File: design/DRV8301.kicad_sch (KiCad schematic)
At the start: 40 parts, among them U2 LM3671, U3 DRV8301

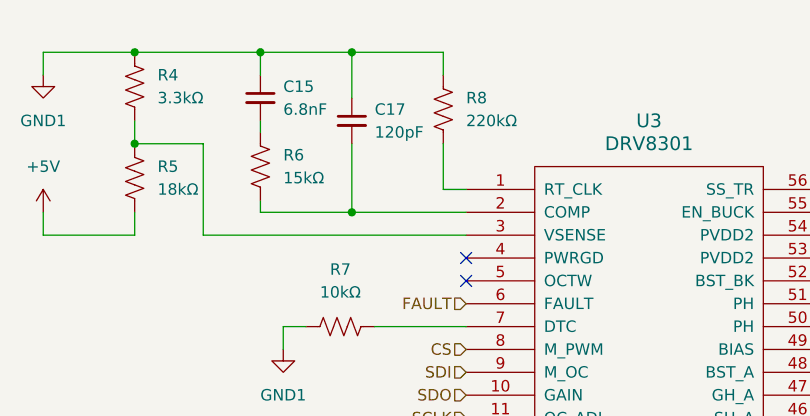
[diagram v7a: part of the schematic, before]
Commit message: Cambios
Actualizado footprint de USB, cambio de capacitor de feedback por uno básico, pequeños cambios en la ubicación de los footprints.
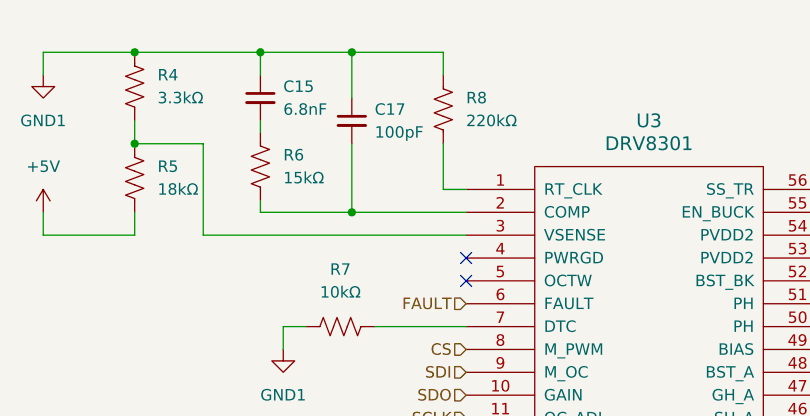
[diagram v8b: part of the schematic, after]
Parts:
- C12: MPN CL10A475KO8NNNC -> (none); Manufacturer Samsung Electro-Mechanics -> (none)
- C13, C14, C16, C18, C20, C29: MPN CL10A225KO8NNNC -> (none); Manufacturer Samsung Electro-Mechanics -> (none)
- C15: MPN CC1206KKX7RCBB682 -> (none); Manufacturer YAGEO -> (none)
- C17: value 120pF -> 100pF; LCSC C3852667 -> C14858; MPN CC0603JRNPOYBN121 -> (none); Manufacturer YAGEO -> (none)
- C19: MPN CL10B223KC8WPNC -> (none); Manufacturer Samsung Electro-Mechanics -> (none)
- C21, C30: MPN CL31A107MQHNNNE -> (none); Manufacturer Samsung Electro-Mechanics -> (none)
- C22, C28: MPN C1210X475K101T -> (none); Manufacturer Holy Stone Enterprise Co., Ltd. -> (none)
- C23, C24, C27: MPN CL10B224KA8NNNC -> (none); Manufacturer Samsung Electro-Mechanics -> (none)
- C25: MPN CC0603KRX7R8BB153 -> (none); Manufacturer YAGEO -> (none)
- C26: MPN CC0603KRX7R9BB104 -> (none); Manufacturer YAGEO -> (none)
- D4: MPN SS54 -> (none); Manufacturer MDD(Microdiode Semiconductor) -> (none)
- D5: MPN SML-310VTT86 -> (none); Manufacturer ROHM Semicon -> (none)
- L1: MPN WI0603LD2R2MST-TIA-HF -> (none); Manufacturer DDY -> (none)
- L2: MPN AHW1608FE220KTF -> (none); Manufacturer APV -> (none)
- R10, R11, R9: MPN RC0603FR-0739KL -> (none); Manufacturer YAGEO -> (none)
- R12, R14, R15: MPN AC0603DR-072K2L -> (none); Manufacturer YAGEO -> (none)
- R13: MPN RM06F1500CT -> (none); Manufacturer CAL-CHIP ELECTRONICS, INC. -> (none)
- R4: MPN 0603WAF3301T5E -> (none); Manufacturer UNI-ROYAL(Uniroyal Elec) -> (none)
- R5: MPN 0603WAF1802T5E -> (none); Manufacturer UNI-ROYAL(Uniroyal Elec) -> (none)
- R6: MPN 0603WAF1502T5E -> (none); Manufacturer UNI-ROYAL(Uniroyal Elec) -> (none)
- R7: MPN RC0603FR-0710KL -> (none); Manufacturer YAGEO -> (none)
- R8: MPN RC0603FR-07220KL -> (none); Manufacturer YAGEO -> (none)
- TP11, TP12, TP13: now left out of the parts list
- U2: MPN LM3671MF-1.2/NOPB -> (none); Manufacturer Texas Instruments -> (none)
- U3: MPN DRV8301DCAR -> (none); Manufacturer Texas Instruments -> (none)
